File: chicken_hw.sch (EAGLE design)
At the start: 13 parts

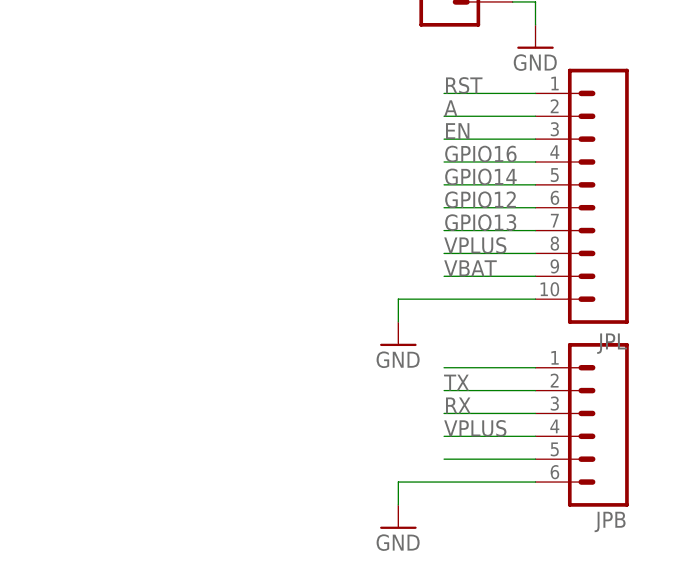
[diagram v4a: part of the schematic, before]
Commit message: Add two leds to gpio 16,14 for easy status
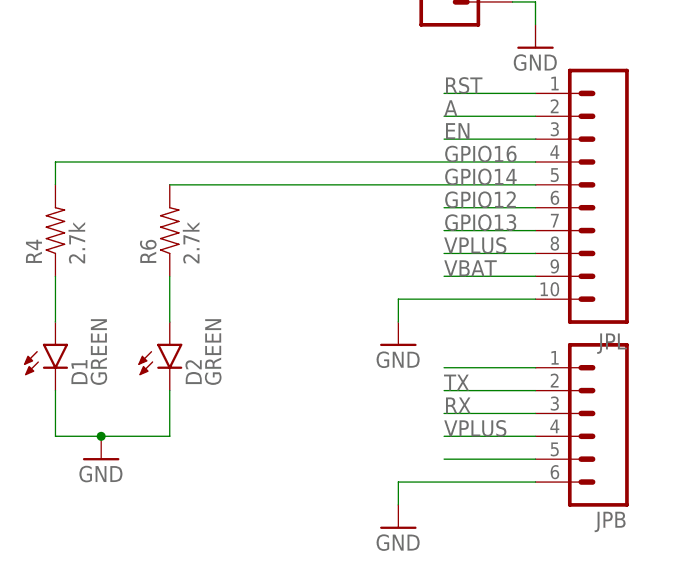
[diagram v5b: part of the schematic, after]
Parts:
- added D1, D2: GREEN, SparkFun-LED:LED-GREEN0603
- added R4, R6: 2.7k, SparkFun-Resistors:RESISTOR0603
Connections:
- new net N$8: D1.A, R4.1
- new net N$9: D2.A, R6.1
- net GND: now also D1.C, D2.C
- net GPIO14: now also R6.2
- net GPIO16: now also R4.2
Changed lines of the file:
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@@
 <part name="R3" library="SparkFun-Resistors" deviceset="RESISTOR" device="0603" value="10k"/>
 <part name="R2" library="SparkFun-Resistors" deviceset="RESISTOR" device="0603" value="238k"/>
+<part name="D1" library="SparkFun-LED" deviceset="LED-GREEN" device="0603" value="GREEN"/>
+<part name="D2" library="SparkFun-LED" deviceset="LED-GREEN" device="0603" value="GREEN"/>
+<part name="GND11" library="SparkFun-Aesthetics" deviceset="GND" device=""/>
+<part name="R4" library="SparkFun-Resistors" deviceset="RESISTOR" device="0603" value="2.7k"/>
+<part name="R6" library="SparkFun-Resistors" deviceset="RESISTOR" device="0603" value="2.7k"/>
 </parts>
 <sheets>
@@
 <instance part="R3" gate="G$1" x="73.66" y="60.96" rot="R90"/>
 <instance part="R2" gate="G$1" x="99.06" y="76.2" rot="R90"/>
+<instance part="D1" gate="G$1" x="-53.34" y="17.78"/>
+<instance part="D2" gate="G$1" x="-40.64" y="17.78"/>
+<instance part="GND11" gate="1" x="-48.26" y="5.08"/>
+<instance part="R4" gate="G$1" x="-53.34" y="30.48" rot="R90"/>
+<instance part="R6" gate="G$1" x="-40.64" y="30.48" rot="R90"/>
 </instances>
 <busses>
@@
 <segment>
 <pinref part="JPL" gate="G$1" pin="4"/>
-<wire x1="0" y1="38.1" x2="-10.16" y2="38.1" width="0.1524" layer="91"/>
 <label x="-10.16" y="38.1" size="1.778" layer="95"/>
+<wire x1="0" y1="38.1" x2="-53.34" y2="38.1" width="0.1524" layer="91"/>
+<pinref part="R4" gate="G$1" pin="2"/>
+<wire x1="-53.34" y1="38.1" x2="-53.34" y2="35.56" width="0.1524" layer="91"/>
 </segment>
 </net>
@@
 <segment>
 <pinref part="JPL" gate="G$1" pin="5"/>
-<wire x1="0" y1="35.56" x2="-10.16" y2="35.56" width="0.1524" layer="91"/>
 <label x="-10.16" y="35.56" size="1.778" layer="95"/>
+<pinref part="R6" gate="G$1" pin="2"/>
+<wire x1="0" y1="35.56" x2="-40.64" y2="35.56" width="0.1524" layer="91"/>
 </segment>
 </net>
@@
 <wire x1="109.22" y1="71.12" x2="109.22" y2="73.66" width="0.1524" layer="91"/>
 </segment>
+<segment>
+<pinref part="D1" gate="G$1" pin="C"/>
+<wire x1="-53.34" y1="12.7" x2="-53.34" y2="7.62" width="0.1524" layer="91"/>
+<pinref part="GND11" gate="1" pin="GND"/>
+<wire x1="-53.34" y1="7.62" x2="-48.26" y2="7.62" width="0.1524" layer="91"/>
+<wire x1="-48.26" y1="7.62" x2="-40.64" y2="7.62" width="0.1524" layer="91"/>
+<junction x="-48.26" y="7.62"/>
+<pinref part="D2" gate="G$1" pin="C"/>
+<wire x1="-40.64" y1="7.62" x2="-40.64" y2="12.7" width="0.1524" layer="91"/>
+</segment>
 </net>
 <net name="N$11" class="0">
@@
 </segment>
 </net>
+<net name="N$8" class="0">
+<segment>
+<pinref part="R4" gate="G$1" pin="1"/>
+<pinref part="D1" gate="G$1" pin="A"/>
+<wire x1="-53.34" y1="25.4" x2="-53.34" y2="20.32" width="0.1524" layer="91"/>
+</segment>
+</net>
+<net name="N$9" class="0">
+<segment>
+<pinref part="R6" gate="G$1" pin="1"/>
+<pinref part="D2" gate="G$1" pin="A"/>
+<wire x1="-40.64" y1="25.4" x2="-40.64" y2="20.32" width="0.1524" layer="91"/>
+</segment>
+</net>

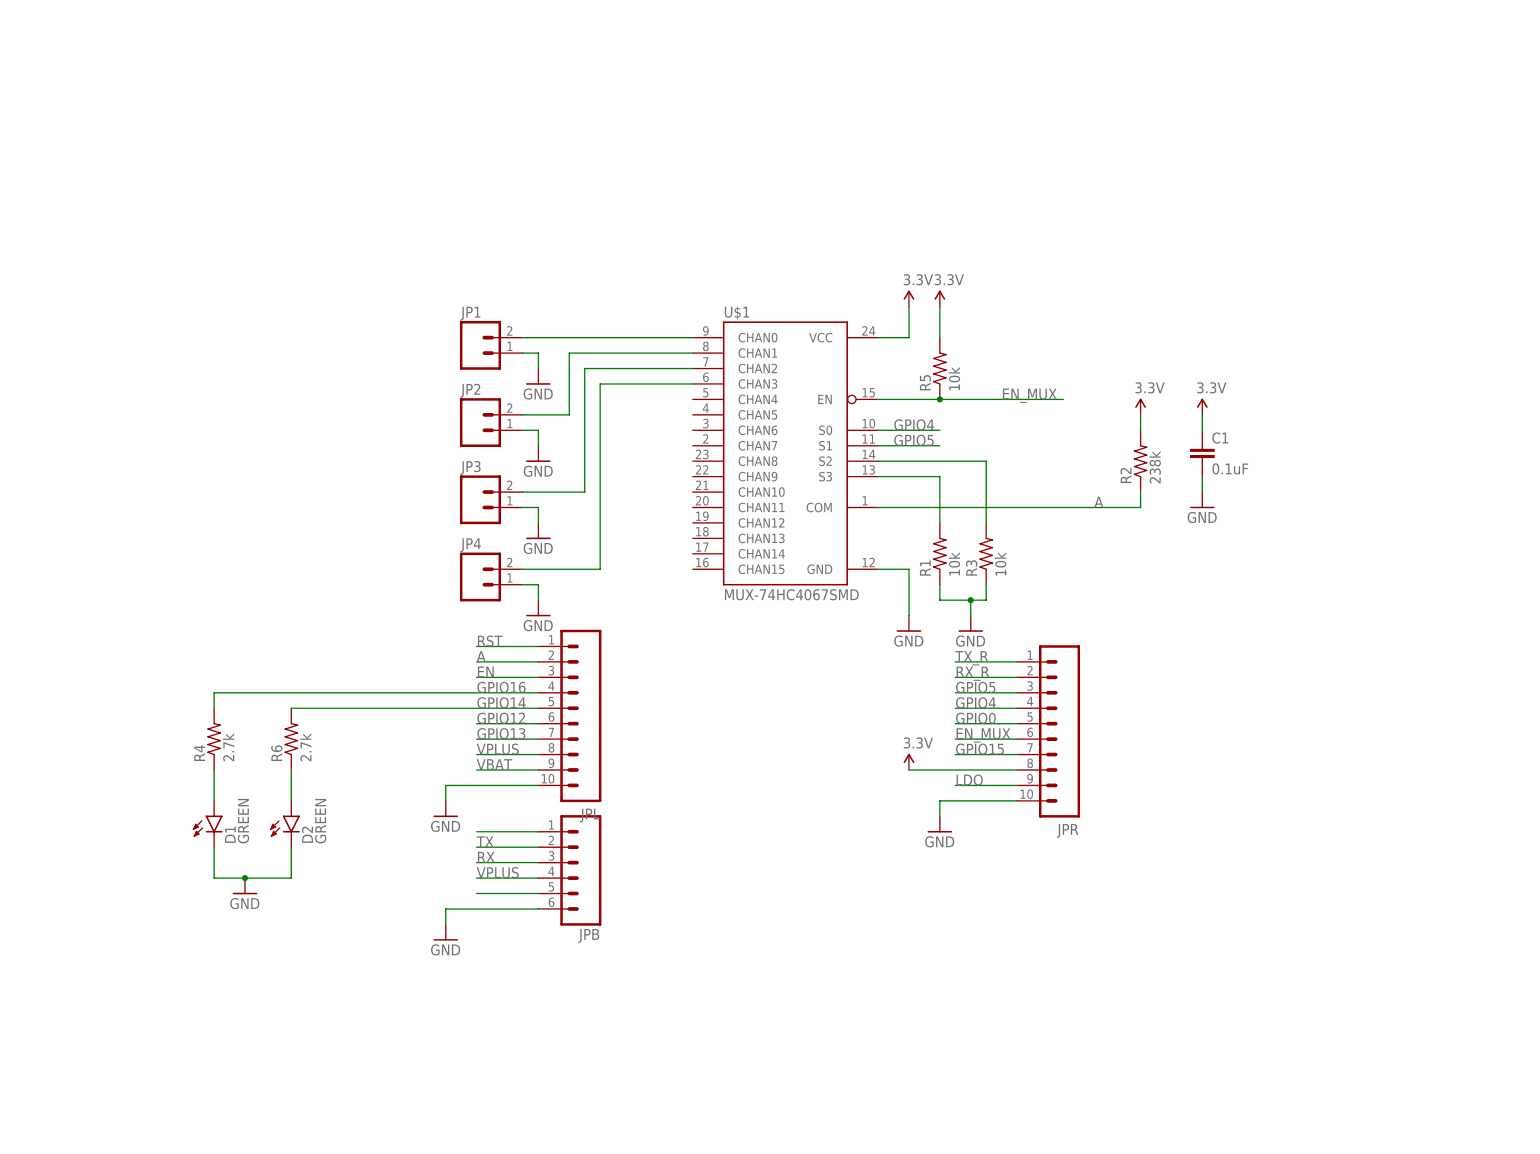
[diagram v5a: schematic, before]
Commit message: Add designer information and schematic frame
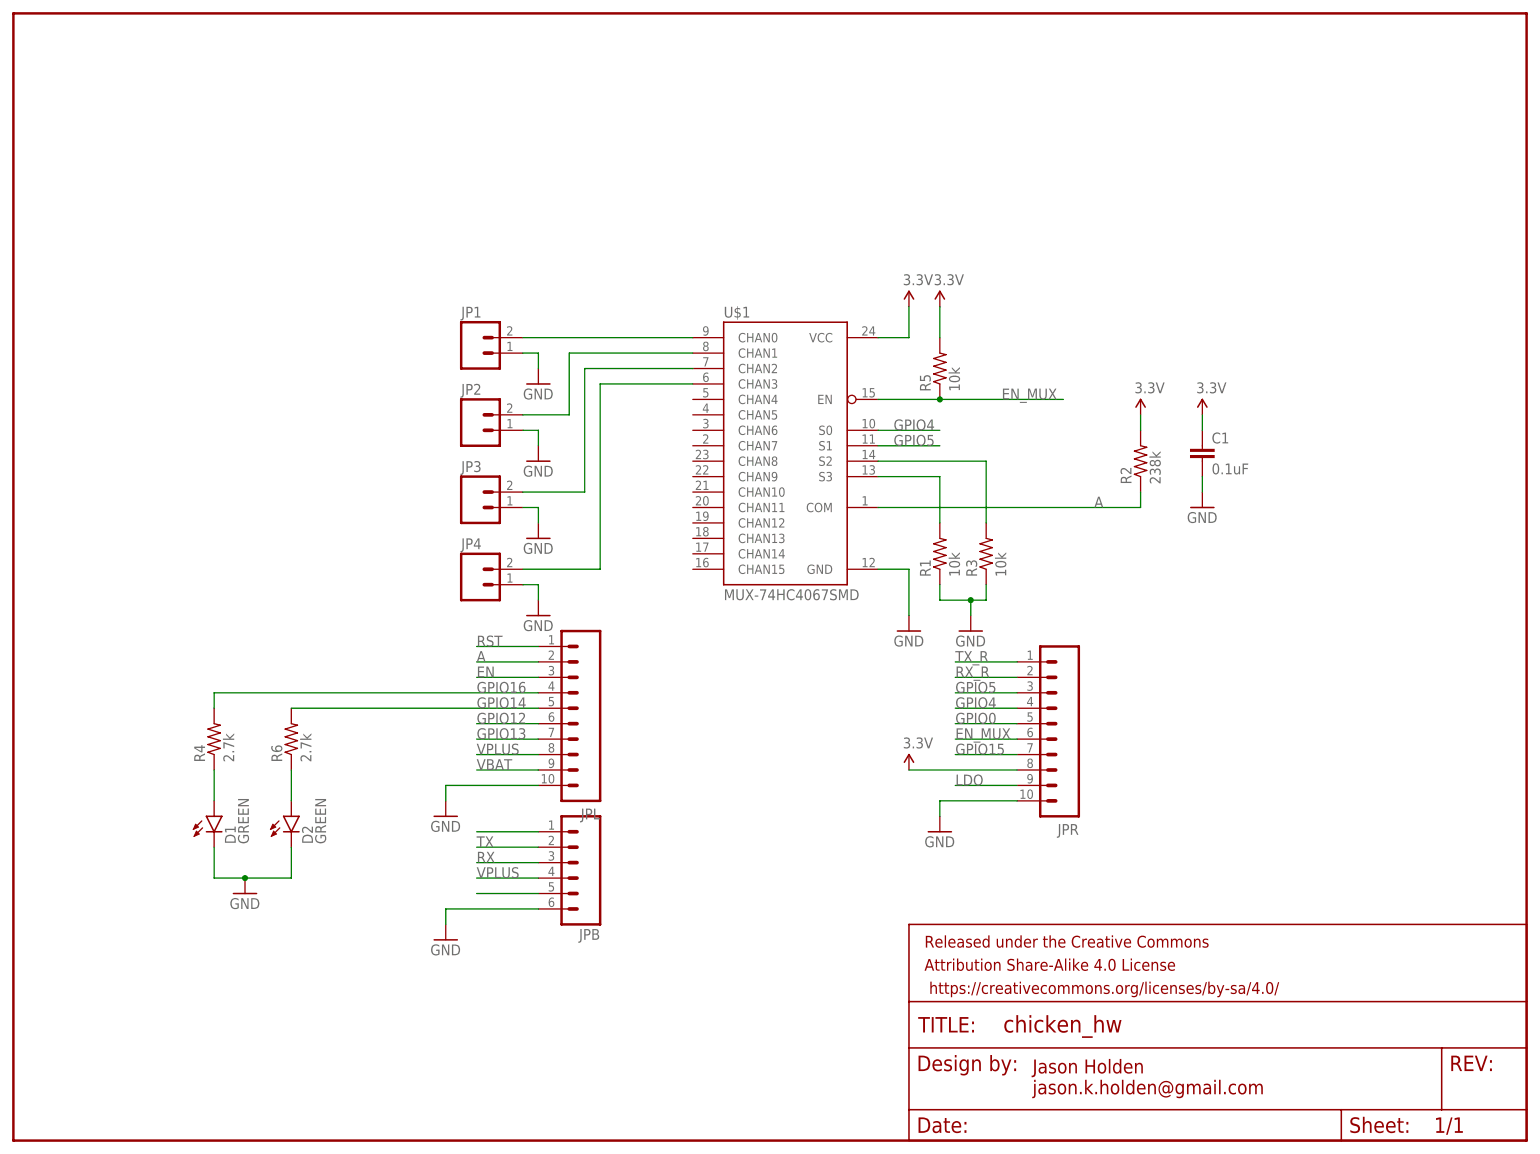
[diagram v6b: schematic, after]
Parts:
- added FRAME1: FRAME-LETTER, SparkFun-Aesthetics:FRAME-LETTER
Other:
- note added: "Jason Holden jason.k.holden@gmail.com"
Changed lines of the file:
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@@
 <part name="R4" library="SparkFun-Resistors" deviceset="RESISTOR" device="0603" value="2.7k"/>
 <part name="R6" library="SparkFun-Resistors" deviceset="RESISTOR" device="0603" value="2.7k"/>
+<part name="FRAME1" library="SparkFun-Aesthetics" deviceset="FRAME-LETTER" device=""/>
 </parts>
 <sheets>
 <sheet>
 <plain>
+<text x="81.28" y="-27.94" size="2.286" layer="94" font="vector" ratio="12">Jason Holden
+jason.k.holden@gmail.com</text>
 </plain>
 <instances>
@@
 <instance part="R4" gate="G$1" x="-53.34" y="30.48" rot="R90"/>
 <instance part="R6" gate="G$1" x="-40.64" y="30.48" rot="R90"/>
+<instance part="FRAME1" gate="G$1" x="-86.36" y="-35.56"/>
+<instance part="FRAME1" gate="V" x="60.96" y="-35.56"/>
 </instances>
 <busses>
@@
 </schematic>
 </drawing>
+<compatibility>
+<note version="6.3" minversion="6.2.2" severity="warning">
+Since Version 6.2.2 text objects can contain more than one line,
+which will not be processed correctly with this version.
+</note>
+</compatibility>
 </eagle>

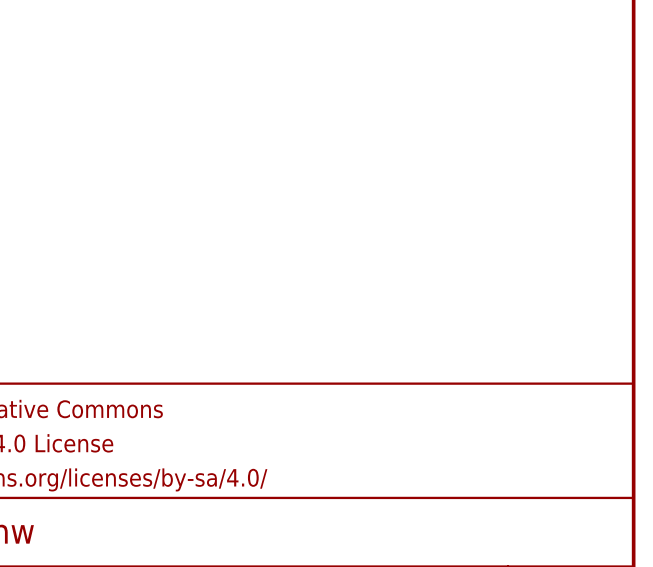
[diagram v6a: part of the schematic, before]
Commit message: Add open source hardware logo and bottom silk
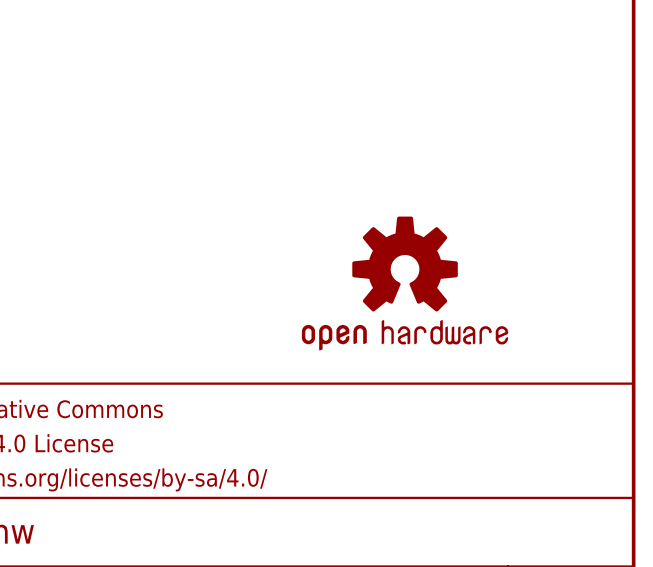
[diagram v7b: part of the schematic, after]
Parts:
- added LOGO1: OSHW-LOGOS, SparkFun-Aesthetics:OSHW-LOGOS
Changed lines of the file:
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@@
 <part name="R6" library="SparkFun-Resistors" deviceset="RESISTOR" device="0603" value="2.7k"/>
 <part name="FRAME1" library="SparkFun-Aesthetics" deviceset="FRAME-LETTER" device=""/>
+<part name="LOGO1" library="SparkFun-Aesthetics" deviceset="OSHW-LOGO" device="S"/>
 </parts>
 <sheets>
@@
 <instance part="FRAME1" gate="G$1" x="-86.36" y="-35.56"/>
 <instance part="FRAME1" gate="V" x="60.96" y="-35.56"/>
+<instance part="LOGO1" gate="G$1" x="137.16" y="12.7"/>
 </instances>
 <busses>
